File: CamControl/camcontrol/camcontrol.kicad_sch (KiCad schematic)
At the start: 45 parts

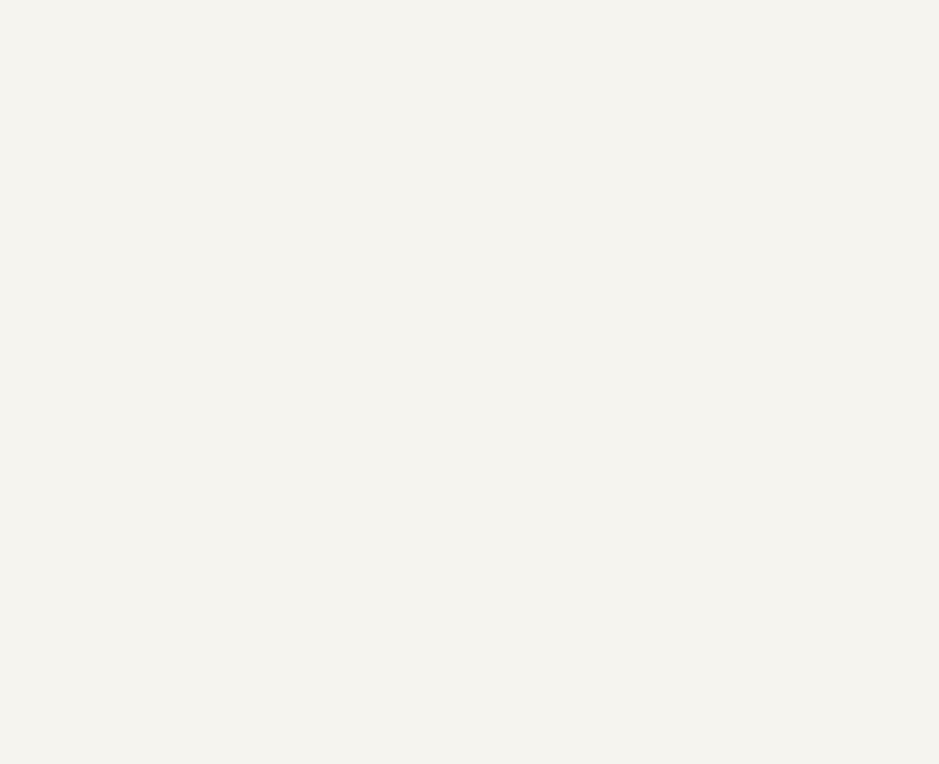
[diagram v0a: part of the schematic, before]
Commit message: it doesnt work - tryied to write custom library
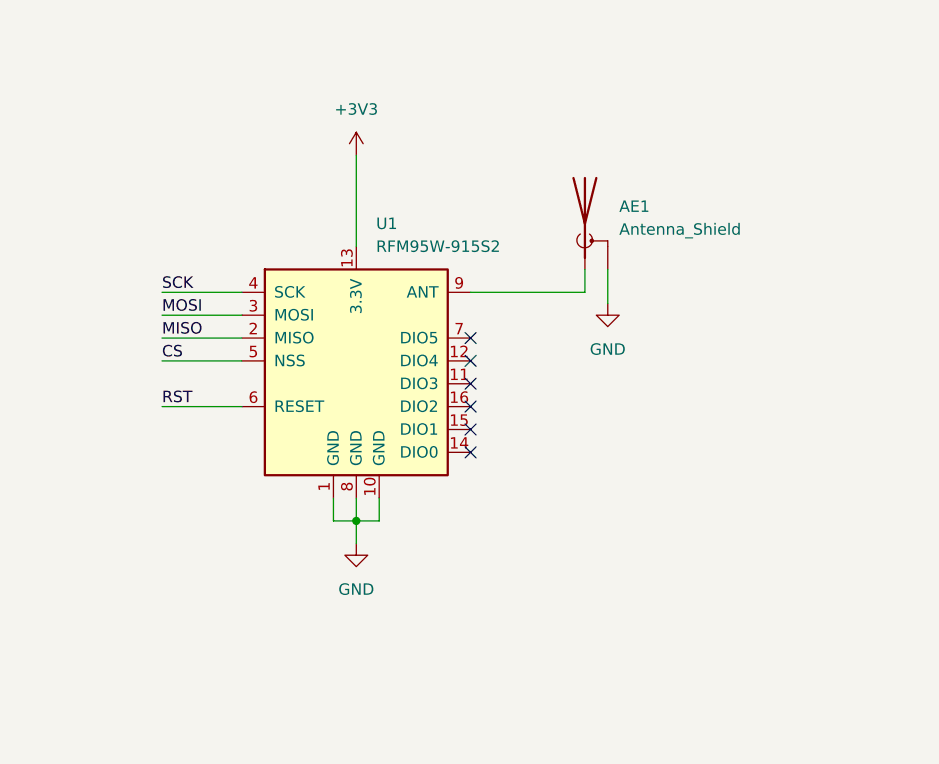
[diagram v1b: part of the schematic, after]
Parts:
- added AE1: Antenna_Shield, .pretty:CONN-SMD_KH-SMA-KE8-G, symbol Device:Antenna_Shield
- added U1: RFM95W-915S2, symbol RF_Module:RFM95W-915S2
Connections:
- net +3V3: now also U1.13 (3.3V)
- net GND: now also AE1.2 (Shield), U1.1 (GND), U1.10 (GND), U1.8 (GND)
- new net: AE1.1 (A), U1.9 (ANT)
- new net CS: U1.5 (NSS)
- new net MISO: U1.2 (MISO)
- new net MOSI: U1.3 (MOSI)
- new net RST: U1.6 (RESET)
- new net SCK: U1.4 (SCK)
- no-connect marks 25 -> 31

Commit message: cam control
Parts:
- removed C? (x12): 100n, Capacitor_SMD:C_0402_1005Metric, symbol Device:C_Small
- removed C? (x4): 1u, Capacitor_SMD:C_0402_1005Metric, symbol Device:C_Small
- removed C?: 10u, Capacitor_SMD:C_0603_1608Metric, symbol Device:C_Small
- removed D? (x2): LED, LED_SMD:LED_0805_2012Metric, symbol Device:LED
- removed D?: D_Schottky, Diode_SMD:D_SOD-323F, symbol Device:D_Schottky
- removed H? (x2): MountingHole_Pad, MountingHole:MountingHole_2.2mm_M2_DIN965_Pad, symbol Mechanical:MountingHole_Pad
- removed J?: Conn_01x02, Jumper:SolderJumper-2_P1.3mm_Open_RoundedPad1.0x1.5mm, symbol Connector_Generic:Conn_01x02
- removed J?: USB_B_Micro, easyeda2kicad:MICRO-USB-SMD_U254-051T-4BHJ25-F2S, symbol Connector:USB_B_Micro
- removed J?: Conn_01x02, Jumper:SolderJumper-2_P1.3mm_Open_Pad1.0x1.5mm, symbol Connector_Generic:Conn_01x02
- removed J?: Screw_Terminal_01x02, TerminalBlock_Phoenix:TerminalBlock_Phoenix_MPT-0,5-2-2.54_1x02_P2.54mm_Horizontal, symbol Connector:Screw_Terminal_01x02
- removed Q? (x2): AO3401A, Package_TO_SOT_SMD:SOT-23, symbol Transistor_FET:AO3401A
- removed R? (x3): 1k, Resistor_SMD:R_0402_1005Metric, symbol Device:R_Small
- removed R?: 30k, Resistor_SMD:R_0402_1005Metric, symbol Device:R_Small
- removed R?: R_Small, symbol Device:R_Small
- removed R? (x3): 5.1k, Resistor_SMD:R_0402_1005Metric, symbol Device:R_Small
- removed R? (x2): 22R, Resistor_SMD:R_0402_1005Metric, symbol Device:R_Small
- removed R?: 51k, Resistor_SMD:R_0402_1005Metric, symbol Device:R_Small
- removed TP?: TestPoint, TestPoint:TestPoint_Pad_1.0x1.0mm, symbol Connector:TestPoint
- removed U1: RFM95W-915S2, symbol RF_Module:RFM95W-915S2
- removed U?: ADS1015IDGS, Package_SO:TSSOP-10_3x3mm_P0.5mm, symbol Analog_ADC:ADS1015IDGS
- removed U?: RP2040, Package_DFN_QFN:QFN-56-1EP_7x7mm_P0.4mm_EP3.2x3.2mm, symbol MCU_RaspberryPi:RP2040
- removed U?: XC6206P332MR, :SOT-23-3_L2.9-W1.6-P1.90-LS2.8-BR, symbol .kicad_sym:XC6206P332MR
- removed U?: W25Q128JVS, Package_SO:SOIC-8_5.23x5.23mm_P1.27mm, symbol Memory_Flash:W25Q128JVS
- removed X?: SX1M12.000M10F30TNN, easyeda2kicad:OSC-SMD_4P-L2.0-W1.6-BL, symbol easyeda2kicad:SX1M12.000M10F30TNN
- added C1, C10, C12, C14, C17, C18, C19, C20, C21, C22, C29, C4, C7: 100n, Capacitor_SMD:C_0402_1005Metric, symbol Device:C_Small
- added C11, C3, C9: 10u, Capacitor_SMD:C_0603_1608Metric, symbol Device:C_Small
- added C13, C15, C5, C6: 1u, Capacitor_SMD:C_0402_1005Metric, symbol Device:C_Small
- added C2: 10n, Capacitor_SMD:C_0402_1005Metric, symbol Device:C_Small
- added C23, C24, C25: 22u, Capacitor_SMD:C_0603_1608Metric, symbol Device:C_Small
- added C26, C28: 220n, Capacitor_SMD:C_0402_1005Metric, symbol Device:C_Small
- added C27, C30: 22n, Capacitor_SMD:C_0402_1005Metric, symbol Device:C_Small
- added C8: 10p, Capacitor_SMD:C_0402_1005Metric, symbol Device:C_Small
- added D1, D3: LED, LED_SMD:LED_0603_1608Metric, symbol Device:LED
- added D4: D_Schottky, Diode_SMD:D_SOD-323F, symbol Device:D_Schottky
- added H1, H2: MountingHole_Pad, MountingHole:MountingHole_2.2mm_M2_DIN965_Pad, symbol Mechanical:MountingHole_Pad
- added J2: USB_B_Micro, easyeda2kicad2:MICRO-USB-SMD_U254-051T-4BHJ25-F2S, symbol Connector:USB_B_Micro
- added J3, J7: Conn_01x03, footprints:CONN3_2059-303&slash_998-403_WAG, symbol Connector_Generic:Conn_01x03
- added J4: Conn_01x02, SamacSys_Parts:PKMCS0909E4000R1, symbol Connector_Generic:Conn_01x02
- added J5: Conn_01x02, Jumper:SolderJumper-2_P1.3mm_Open_Pad1.0x1.5mm, symbol Connector_Generic:Conn_01x02
- added J6: Conn_01x02, Jumper:SolderJumper-2_P1.3mm_Open_RoundedPad1.0x1.5mm, symbol Connector_Generic:Conn_01x02
- added J8: Conn_01x04, Connector_JST:JST_EH_B4B-EH-A_1x04_P2.50mm_Vertical, symbol Connector_Generic:Conn_01x04
- added L1: 1uH, Inductor_SMD:L_1008_2520Metric, symbol Device:L_Small
- added Q2, Q3: AO3401A, Package_TO_SOT_SMD:SOT-23, symbol Transistor_FET:AO3401A
- added R1, R3, R9: 1k, Resistor_SMD:R_0402_1005Metric, symbol Device:R_Small
- added R10: 111k, Resistor_SMD:R_0603_1608Metric, symbol Device:R_Small
- added R11, R20: Rsns, Resistor_SMD:R_0402_1005Metric, symbol Device:R_Small
- added R12, R21: 50k, Resistor_SMD:R_0402_1005Metric, symbol Device:R_Small
- added R13, R2: 1M, Resistor_SMD:R_0402_1005Metric, symbol Device:R_Small
- added R14, R15, R16, R17, R18, R19, R6: 5.1k, Resistor_SMD:R_0402_1005Metric, symbol Device:R_Small
- added R4, R5: 22R, Resistor_SMD:R_0402_1005Metric, symbol Device:R_Small
- added R7: 27k, Resistor_SMD:R_0402_1005Metric, symbol Device:R_Small
- added R8: 51k, Resistor_SMD:R_0402_1005Metric, symbol Device:R_Small
- added U1: E22-900MM22S, .pretty:WIRELM-SMD_E22-400MM22S, symbol .kicad_sym:E22-400MM22S
- added U2, U7: TPS1HC30BQPWPRQ1, .pretty:HTSSOP-14_L5.0-W4.4-P0.65-LS6.4-BL-EP-3, symbol .kicad_sym:TPS1HC30BQPWPRQ1
- added U3: TPS63060DSCR, .pretty:WSON-10_L3.0-W3.0-P0.50-BL-EP-A, symbol .kicad_sym:TPS63060DSCR
- added U4: XC6206P332MR, Package_TO_SOT_SMD:SOT-23-3, symbol .kicad_sym:XC6206P332MR
- added U5: W25Q128JVS, Package_SO:SOIC-8_5.3x5.3mm_P1.27mm, symbol Memory_Flash:W25Q128JVS
- added U6: RP2040, Package_DFN_QFN:QFN-56-1EP_7x7mm_P0.4mm_EP3.2x3.2mm, symbol MCU_RaspberryPi:RP2040
- added X1: SX1M12.000M10F30TNN, easyeda2kicad2:OSC-SMD_4P-L2.0-W1.6-BL, symbol easyeda2kicad:SX1M12.000M10F30TNN
- AE1: footprint .pretty:CONN-SMD_KH-SMA-KE8-G -> .pretty:ANT-SMD_1909763-1; LCSC Part C530661 -> C392444
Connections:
- net +1V1: now also C10.1, C13.1, U6.23 (DVDD), U6.45 (VREG_VOUT), U6.50 (DVDD)
- net +3V3: now also C12.1, C14.1, C15.1, C17.1, C18.1, C19.1, C2.1, C20.1, C21.1, C22.1, C3.1, C6.1, D3.2 (A), R1.2, R6.1, U1.1 (VCC), U4.2 (Vout), U5.8 (VCC), U6.1 (IOVDD), U6.10 (IOVDD), U6.22 (IOVDD), U6.33 (IOVDD), U6.42 (IOVDD), U6.43 (ADC_AVDD), U6.44 (VREG_IN), U6.48 (USB_VDD), U6.49 (IOVDD), X1.1 (OE/NC), X1.4 (VDD)
- net +BATT: now also J7.3 (Pin_2), J7.4 (Pin_2), Q2.3 (D)
- net BATT POSTSW: now also C11.1, C9.1, Q2.2 (S), Q3.3 (D), R7.1, U3.2 (VIN), U3.3 (EN)
- net BOOTSEL: now also J6.2 (Pin_2), R3.2
- net GND: now also C1.2, C10.2, C11.2, C12.2, C13.2, C14.2, C15.2, C17.2, C18.2, C19.2, C2.2, C20.2, C21.2, C22.2, C23.2, C24.2, C25.2, C26.2, C27.2, C28.2, C29.2, C3.2, C30.2, C4.2, C5.2, C6.2, C7.2, C8.2, C9.2, D1.1 (K), H1.1, H2.1, J2.5 (GND), J3.3 (Pin_2), J3.4 (Pin_2), J4.2 (Pin_2), J6.1 (Pin_1), J7.1 (Pin_1), J7.2 (Pin_1), J7.5 (Pin_3), J7.6 (Pin_3), J8.3 (Pin_3), Q2.1 (G), R10.2, R11.2, R12.2, R20.2, R21.2, R8.2, U1.16 (GND), U1.2 (GND), U1.7 (GND), U2.1 (GND), U2.15 (GND), U3.11 (PAD), U3.4 (PS/SYNC), U3.7 (GND), U4.1 (GND), U5.4 (GND), U6.19 (TESTEN), U6.57 (GND), U7.1 (GND), U7.15 (GND), X1.2 (GND)
- net LEDINDICATION: now also R9.1, U6.11 (GPIO8)
- net MISO: now also U1.12 (MISO), U6.27 (GPIO16)
- net MOSI: now also U1.13 (MOSI), U6.30 (GPIO19)
- net QSPI_SCLK: now also U5.6 (CLK), U6.52 (QSPI_SCLK)
- net QSPI_SD1: now also U5.2 (DO/IO_{1}), U6.55 (QSPI_SD1)
- net QSPI_SD2: now also U5.3 (~{WP}/IO_{2}), U6.54 (QSPI_SD2)
- net QSPI_SD3: now also U5.7 (~{HOLD}/~{RESET}/IO_{3}), U6.51 (QSPI_SD3)
- net QSPI_SDO: now also U5.5 (DI/IO_{0}), U6.53 (QSPI_SD0)
- net QSPI_SS: now also R3.1, U5.1 (~{CS}), U6.56 (QSPI_SS)
- net RP USB_D+: now also R4.2, U6.47 (USB_DP)
- net RP USB_D-: now also R5.1, U6.46 (USB_DM)
- net RUN: now also R6.2, U6.26 (RUN)
- net SWCLK: now also J5.1 (Pin_1), U6.24 (SWCLK)
- net SWD: now also J5.2 (Pin_2), U6.25 (SWD)
- net USB_D+: now also J2.3 (D+), R4.1
- net USB_D-: now also J2.2 (D-), R5.2
- net VBUS: now also D4.2 (A), J2.1 (VBUS), Q3.1 (G)
- net XIN: now also U6.20 (XIN), X1.3 (OUT)
- net at AE1.1 (A): now also U1.6 (ANT)
- new net: C8.1, R10.1, R2.2, U3.8 (FB)
- new net: R19.2, R20.1, U7.6 (SNS)
- new net: C5.1, D4.1 (K), Q3.2 (S), U4.3 (Vin)
- new net: D1.2 (A), R1.1
- new net: R21.1, U7.7 (ILIM)
- new net: L1.1, U3.1 (L1)
- new net: L1.2, U3.10 (L2)
- new net: D3.1 (K), R9.2
- new net: R15.2, U2.2 (EN)
- new net: R17.2, U7.2 (EN)
- new net: R18.2, U7.3 (DIAG_EN)
- new net: R16.2, U2.3 (DIAG_EN)
- new net: R11.1, R14.2, U2.6 (SNS)
- new net: R12.1, U2.7 (ILIM)
- new net: R13.2, U3.5 (PG)
- new net: C7.1, U3.6 (VAUX)
- new net +12V: C28.1, C29.1, J3.5 (Pin_3), J3.6 (Pin_3), U7.12 (VBB), U7.13 (VBB)
- new net +5V: C23.1, C24.1, C25.1, C26.1, C4.1, R13.1, R2.1, U2.12 (VBB), U2.13 (VBB), U3.9 (VOUT)
- new net BUSY: U1.11 (BUSY)
- new net BUZZER: J4.1 (Pin_1)
- new net CAM BATT SENSE : R7.2, R8.1, U6.41 (GPIO29_ADC3)
- new net CAM DIAG EN: R16.1
- new net CAM EN: R15.1
- new net CAM RX: J8.1 (Pin_1)
- new net CAM TX: J8.2 (Pin_2)
- new net CAMPWR: C27.1, J8.4 (Pin_4), U2.10 (VOUT), U2.9 (VOUT)
- new net CAMSNS: R14.1, U6.40 (GPIO28_ADC2)
- new net RXEN: U1.10 (RXEN)
- new net SCLK: U1.15 (SCK), U6.29 (GPIO18)
- new net SX CS: U1.14 (NSS)
- new net SX RST: C1.1, U1.3 (NRST)
- new net TX BATT SENSE : U6.38 (GPIO26_ADC0)
- new net TXEN: U1.9 (TXEN)
- new net VID DIAG EN: R18.1
- new net VID EN: R17.1
- new net VIDPWR: C30.1, J3.1 (Pin_1), J3.2 (Pin_1), U7.10 (VOUT), U7.9 (VOUT)
- new net VIDSNS: R19.1, U6.39 (GPIO27_ADC1)
- no-connect marks 31 -> 37
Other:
- note added: "3v3 LDO"
- note added: "5V BUCK-BOOST"
- note added: "BUZZER"
- note added: "CAM SWITCH / CURRENT SENSE"
- note added: "CONNECTORS"
- note added: "Camera UART"
- note added: "RADIO"
- note added: "VID SWITCH/CURRENT SENSE"
- note removed: "ADC"
- note removed: "POWER"

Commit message: first routing pass
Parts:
- removed C2: 10n, Capacitor_SMD:C_0402_1005Metric, symbol Device:C_Small
- removed C3: 10u, Capacitor_SMD:C_0603_1608Metric, symbol Device:C_Small
- removed J4: Conn_01x02, SamacSys_Parts:PKMCS0909E4000R1, symbol Connector_Generic:Conn_01x02
- added D2: LED, LED_SMD:LED_0603_1608Metric, symbol Device:LED
- added R22: 1k, Resistor_SMD:R_0402_1005Metric, symbol Device:R_Small
- added R23: 27k, Resistor_SMD:R_0402_1005Metric, symbol Device:R_Small
- added R24: 51k, Resistor_SMD:R_0402_1005Metric, symbol Device:R_Small
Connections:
- net +12V: now also R23.1
- net +5V: now also Q3.3 (D), R22.2
- net BATT POSTSW: no longer Q3.3 (D)
- net BUSY: now also U6.5 (GPIO3)
- net CAM DIAG EN: now also U6.29 (GPIO18)
- net CAM EN: now also U6.30 (GPIO19)
- net CAM RX: now also U6.27 (GPIO16)
- net CAM TX: now also U6.28 (GPIO17)
- net GND: now also D2.1 (K), R24.2
- net LEDINDICATION: now also U6.14 (GPIO11); no longer U6.11 (GPIO8)
- net MISO: now also U6.31 (GPIO20); no longer U6.27 (GPIO16)
- net MOSI: now also U6.35 (GPIO23); no longer U6.30 (GPIO19)
- net RXEN: now also U6.4 (GPIO2)
- net SCLK: now also U6.34 (GPIO22); no longer U6.29 (GPIO18)
- net SX CS: now also U6.32 (GPIO21)
- net SX RST: now also U6.2 (GPIO0)
- net TX BATT SENSE : now also R23.2, R24.1
- net TXEN: now also U6.3 (GPIO1)
- net VID DIAG EN: now also U6.36 (GPIO24)
- net VID EN: now also U6.37 (GPIO25)
- new net: D2.2 (A), R22.1
- no-connect marks 37 -> 31
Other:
- note added: "Nets are labeled for CAMERA, flipped into MCU"
- note removed: "BUZZER"

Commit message: cam control work and start on gruond station
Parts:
- removed R20: Rsns, Resistor_SMD:R_0402_1005Metric, symbol Device:R_Small
- added R25: 1k, Resistor_SMD:R_0402_1005Metric, symbol Device:R_Small
- C26, C28: LCSC Part C1525 -> C16772
- C27, C30: LCSC Part C1525 -> C1532
- J3, J7, J8: now left out of the parts list
- R11: value Rsns -> 1k; LCSC Part (none) -> C11702
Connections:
- net GND: now also R11.1, R25.1; no longer R11.2
- net at R19.2, U7.6 (SNS): now also R11.2
- net at R14.2, U2.6 (SNS): now also R25.2; no longer R11.1
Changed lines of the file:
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@@
 			)
 		)
-		(property "LCSC Part" "C1525"
+		(property "LCSC Part" "C16772"
 			(at 244.475 33.655 0)
 			(effects
@@
 			)
 		)
-		(property "LCSC Part" "C1525"
+		(property "LCSC Part" "C16772"
 			(at 142.875 38.1 0)
 			(effects
@@
 	(symbol
 		(lib_id "Device:R_Small")
-		(at 245.745 66.675 0)
-		(unit 1)
-		(exclude_from_sim no)
-		(in_bom yes)
-		(on_board yes)
-		(dnp no)
-		(fields_autoplaced yes)
-		(property "Reference" "R20"
-			(at 247.65 65.4049 0)
-			(effects
-				(font
-					(size 1.016 1.016)
-				)
-				(justify left)
-			)
-		)
-		(property "Value" "Rsns"
-			(at 247.65 67.9449 0)
-			(effects
-				(font
-					(size 1.27 1.27)
-				)
-				(justify left)
-			)
-		)
-		(property "Footprint" "Resistor_SMD:R_0402_1005Metric"
-			(at 245.745 66.675 0)
-			(effects
-				(font
-					(size 1.27 1.27)
-				)
-				(hide yes)
-			)
-		)
-		(property "Datasheet" "~"
-			(at 245.745 66.675 0)
-			(effects
-				(font
-					(size 1.27 1.27)
-				)
-				(hide yes)
-			)
-		)
-		(property "Description" "Resistor, small symbol"
-			(at 245.745 66.675 0)
-			(effects
-				(font
-					(size 1.27 1.27)
-				)
-				(hide yes)
-			)
-		)
-		(pin "2"
-		)
-		(pin "1"
-		)
-		(instances
-			(project "camcontrol"
-				(path "/299d0a04-aa0f-4714-a339-a062da4333a5"
-					(reference "R20")
-					(unit 1)
-				)
-			)
-		)
-	)
-	(symbol
-		(lib_id "Device:R_Small")
 		(at 241.3 55.245 90)
 		(unit 1)
@@
 		(unit 1)
 		(exclude_from_sim no)
-		(in_bom yes)
+		(in_bom no)
 		(on_board yes)
 		(dnp no)
@@
 	)
 	(symbol
+		(lib_id "Device:R_Small")
+		(at 144.145 71.12 180)
+		(unit 1)
+		(exclude_from_sim no)
+		(in_bom yes)
+		(on_board yes)
+		(dnp no)
+		(fields_autoplaced yes)
+		(property "Reference" "R25"
+			(at 146.05 70.485 0)
+			(effects
+				(font
+					(size 1.27 1.27)
+				)
+				(justify right)
+			)
+		)
+		(property "Value" "1k"
+			(at 146.05 73.025 0)
+			(effects
+				(font
+					(size 1.27 1.27)
+				)
+				(justify right)
+			)
+		)
+		(property "Footprint" "Resistor_SMD:R_0402_1005Metric"
+			(at 144.145 71.12 0)
+			(effects
+				(font
+					(size 1.27 1.27)
+				)
+				(hide yes)
+			)
+		)
+		(property "Datasheet" "~"
+			(at 144.145 71.12 0)
+			(effects
+				(font
+					(size 1.27 1.27)
+				)
+				(hide yes)
+			)
+		)
+		(property "Description" "Resistor, small symbol"
+			(at 144.145 71.12 0)
+			(effects
+				(font
+					(size 1.27 1.27)
+				)
+				(hide yes)
+			)
+		)
+		(property "LCSC Part" "C11702"
+			(at 144.145 71.12 0)
+			(effects
+				(font
+					(size 1.27 1.27)
+				)
+				(hide yes)
+			)
+		)
+		(property "LCSC_Part" ""
+			(at 144.145 71.12 0)
+			(effects
+				(font
+					(size 1.27 1.27)
+				)
+				(hide yes)
+			)
+		)
+		(pin "1"
+		)
+		(pin "2"
+		)
+		(instances
+			(project "camcontrol"
+				(path "/299d0a04-aa0f-4714-a339-a062da4333a5"
+					(reference "R25")
+					(unit 1)
+				)
+			)
+		)
+	)
+	(symbol
 		(lib_id "power:GND")
 		(at 250.825 214.63 0)
@@
 		(unit 1)
 		(exclude_from_sim no)
-		(in_bom yes)
+		(in_bom no)
 		(on_board yes)
 		(dnp no)
@@
 			)
 		)
-		(property "LCSC Part" "C1525"
+		(property "LCSC Part" "C1532"
 			(at 199.39 46.99 0)
 			(effects
@@
 			)
 		)
-		(property "LCSC Part" "C1525"
+		(property "LCSC Part" "C1532"
 			(at 300.99 42.545 0)
 			(effects
@@
 	)
 	(symbol
-		(lib_id "Device:R_Small")
-		(at 144.145 71.12 0)
-		(unit 1)
-		(exclude_from_sim no)
-		(in_bom yes)
-		(on_board yes)
-		(dnp no)
-		(fields_autoplaced yes)
-		(property "Reference" "R11"
-			(at 146.05 69.8499 0)
-			(effects
-				(font
-					(size 1.016 1.016)
-				)
-				(justify left)
-			)
-		)
-		(property "Value" "Rsns"
-			(at 146.05 72.3899 0)
-			(effects
-				(font
-					(size 1.27 1.27)
-				)
-				(justify left)
-			)
-		)
-		(property "Footprint" "Resistor_SMD:R_0402_1005Metric"
-			(at 144.145 71.12 0)
-			(effects
-				(font
-					(size 1.27 1.27)
-				)
-				(hide yes)
-			)
-		)
-		(property "Datasheet" "~"
-			(at 144.145 71.12 0)
-			(effects
-				(font
-					(size 1.27 1.27)
-				)
-				(hide yes)
-			)
-		)
-		(property "Description" "Resistor, small symbol"
-			(at 144.145 71.12 0)
-			(effects
-				(font
-					(size 1.27 1.27)
-				)
-				(hide yes)
-			)
-		)
-		(pin "2"
-		)
-		(pin "1"
-		)
-		(instances
-			(project ""
-				(path "/299d0a04-aa0f-4714-a339-a062da4333a5"
-					(reference "R11")
-					(unit 1)
-				)
-			)
-		)
-	)
-	(symbol
 		(lib_id "power:+3V3")
 		(at 74.295 170.815 0)
@@
 		(unit 1)
 		(exclude_from_sim no)
-		(in_bom yes)
+		(in_bom no)
 		(on_board yes)
 		(dnp no)
@@
 					(unit 1)
 				)
+			)
+		)
+	)
+	(symbol
+		(lib_id "Device:R_Small")
+		(at 245.745 66.675 180)
+		(unit 1)
+		(exclude_from_sim no)
+		(in_bom yes)
+		(on_board yes)
+		(dnp no)
+		(fields_autoplaced yes)
+		(property "Reference" "R11"
+			(at 247.65 66.04 0)
+			(effects
+				(font
+					(size 1.27 1.27)
+				)
+				(justify right)
+			)
+		)
+		(property "Value" "1k"
+			(at 247.65 68.58 0)
+			(effects
+				(font
+					(size 1.27 1.27)
+				)
+				(justify right)
+			)
+		)
+		(property "Footprint" "Resistor_SMD:R_0402_1005Metric"
+			(at 245.745 66.675 0)
+			(effects
+				(font
+					(size 1.27 1.27)
+				)
+				(hide yes)
+			)
+		)
+		(property "Datasheet" "~"
+			(at 245.745 66.675 0)
+			(effects
+				(font
+					(size 1.27 1.27)
+				)
+				(hide yes)
+			)
+		)
+		(property "Description" "Resistor, small symbol"
+			(at 245.745 66.675 0)
+			(effects
+				(font
+					(size 1.27 1.27)
+				)
+				(hide yes)
+			)
+		)
+		(property "LCSC Part" "C11702"
+			(at 245.745 66.675 0)
+			(effects
+				(font
+					(size 1.27 1.27)
+				)
+				(hide yes)
+			)
+		)
+		(property "LCSC_Part" ""
+			(at 245.745 66.675 0)
+			(effects
+				(font
+					(size 1.27 1.27)
+				)
+				(hide yes)
+			)
+		)
+		(pin "1"
+		)
+		(pin "2"
+		)
+		(instances
+			(project "camcontrol"
+				(path "/299d0a04-aa0f-4714-a339-a062da4333a5"
+					(reference "R11")
+					(unit 1)
+				)

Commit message: cam control rework
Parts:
- removed C1, C7: 100n, Capacitor_SMD:C_0402_1005Metric, symbol Device:C_Small
- removed C11, C9: 10u, Capacitor_SMD:C_0603_1608Metric, symbol Device:C_Small
- removed C23, C24, C25: 22u, Capacitor_SMD:C_0603_1608Metric, symbol Device:C_Small
- removed C8: 10p, Capacitor_SMD:C_0402_1005Metric, symbol Device:C_Small
- removed D2: LED, LED_SMD:LED_0603_1608Metric, symbol Device:LED
- removed J3, J7: Conn_01x03, footprints:CONN3_2059-303&slash_998-403_WAG, symbol Connector_Generic:Conn_01x03
- removed J8: Conn_01x04, Connector_JST:JST_EH_B4B-EH-A_1x04_P2.50mm_Vertical, symbol Connector_Generic:Conn_01x04
- removed L1: 1uH, Inductor_SMD:L_1008_2520Metric, symbol Device:L_Small
- removed R10: 111k, Resistor_SMD:R_0603_1608Metric, symbol Device:R_Small
- removed R13, R2: 1M, Resistor_SMD:R_0402_1005Metric, symbol Device:R_Small
- removed R22: 1k, Resistor_SMD:R_0402_1005Metric, symbol Device:R_Small
- removed U3: TPS63060DSCR, .pretty:WSON-10_L3.0-W3.0-P0.50-BL-EP-A, symbol .kicad_sym:TPS63060DSCR
- added J1, J3, J4, J7: Power 1, .pretty:wago2pin3mmspace, symbol Connector:Screw_Terminal_01x02
- added J8: Conn_01x03, Connector_PinHeader_2.00mm:PinHeader_1x03_P2.00mm_Vertical, symbol Connector_Generic:Conn_01x03
- added JP1: Jumper, Jumper:SolderJumper-3_P1.3mm_Open_RoundedPad1.0x1.5mm, symbol Jumper:SolderJumper_3_Open
- added Q1, Q4: AO3401A, Package_TO_SOT_SMD:SOT-23, symbol Transistor_FET:AO3401A
- C12: now not fitted
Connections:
- net +BATT is gone; now on net +12V: Q2.3 (D)
- net +12V: now also J1.2 (Pin_2), JP1.1 (A); no longer C28.1, C29.1, U7.12 (VBB), U7.13 (VBB)
- net +3V3: now also D1.2 (A); no longer R1.2
- net BUSY: now also U6.30 (GPIO19); no longer U6.5 (GPIO3)
- net CAM BATT SENSE : now also U6.39 (GPIO27_ADC1); no longer U6.41 (GPIO29_ADC3)
- net CAM DIAG EN: now also U6.7 (GPIO5); no longer U6.29 (GPIO18)
- net CAM EN: now also U6.8 (GPIO6); no longer U6.30 (GPIO19)
- net CAM RX: now also J8.1 (Pin_1)
- net CAM TX: now also J8.2 (Pin_2)
- net CAMPWR: now also J7.1 (Pin_1)
- net CAMSNS: now also U6.41 (GPIO29_ADC3); no longer U6.40 (GPIO28_ADC2)
- net GND: now also R1.2, J1.1 (Pin_1), J3.2 (Pin_2), J4.1 (Pin_1), J7.2 (Pin_2), J8.3 (Pin_3), Q1.1 (G), Q4.1 (G); no longer D1.1 (K)
- net RXEN: now also U6.34 (GPIO22); no longer U6.4 (GPIO2)
- net SCLK: now also U6.29 (GPIO18); no longer U6.34 (GPIO22)
- net SX RST: now also U6.37 (GPIO25); no longer U6.2 (GPIO0)
- net TXEN: now also U6.36 (GPIO24); no longer U6.3 (GPIO1)
- net VID DIAG EN: now also U6.4 (GPIO2); no longer U6.36 (GPIO24)
- net VID EN: now also U6.3 (GPIO1); no longer U6.37 (GPIO25)
- net VIDPWR: now also J3.1 (Pin_1)
- net VIDSNS: now also U6.40 (GPIO28_ADC2); no longer U6.39 (GPIO27_ADC1)
- net at C5.1, U4.3 (Vin): now also Q1.2 (S); no longer D4.1 (K), Q3.2 (S)
- net at R1.1: now also D1.1 (K); no longer D1.2 (A)
- net +5V renamed 12VIN
- net 12VIN: now also Q4.2 (S); no longer Q3.3 (D)
- net BATT POSTSW renamed +12VA
- net +12VA: now also J4.2 (Pin_2), JP1.3 (B), Q4.3 (D); no longer Q2.2 (S)
- new net: JP1.2 (C), Q3.3 (D)
- new net: D4.1 (K), Q1.3 (D), Q3.2 (S)
- new net 12VAIN: C28.1, C29.1, Q2.2 (S), U7.12 (VBB), U7.13 (VBB)
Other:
- note removed: "5V BUCK-BOOST"
- moved on the sheet: C5, C6, D1, D4, Q3, R1, R23, R24, U4
